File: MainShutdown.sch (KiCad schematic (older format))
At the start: 21 parts, among them J10 CONN_2X2, J6 CONN_2X2, K1 KT12-1A, K2 G6DN 12V, Q1 SSM3K361TU,LF, Q2 TSM2312, U13 TS3704IPT, U14 CD4044, U15 CD4082, U4 EL5421T

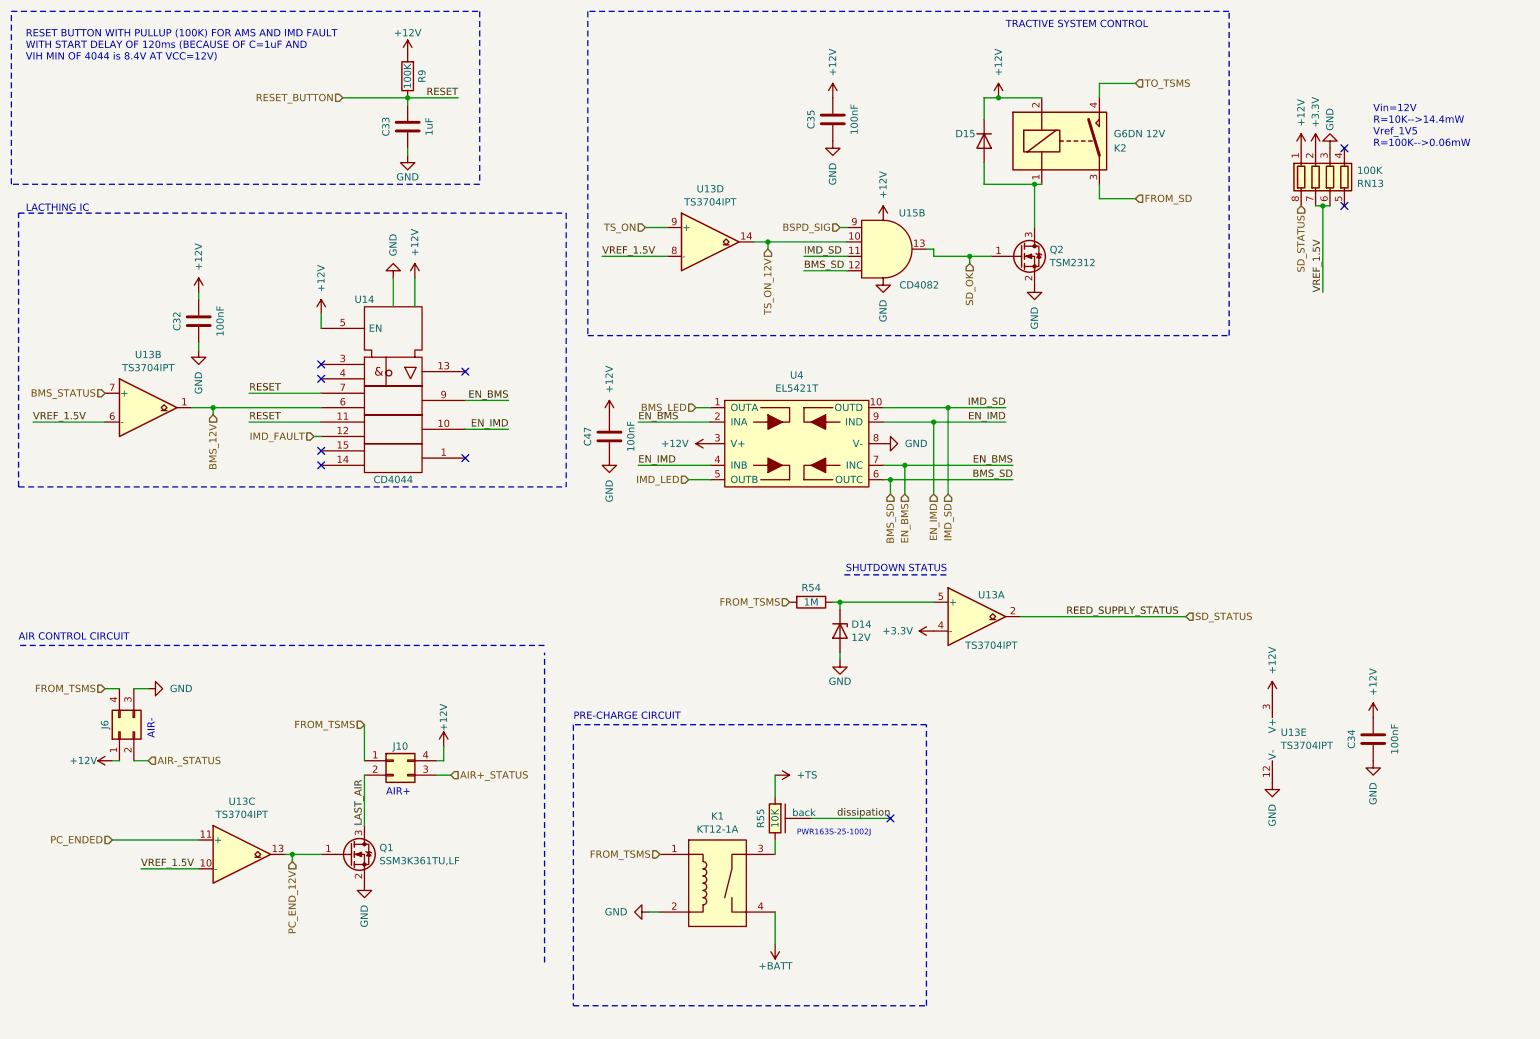
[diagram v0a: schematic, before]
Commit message: added a lot of annotations and readability in the schematic, not complete
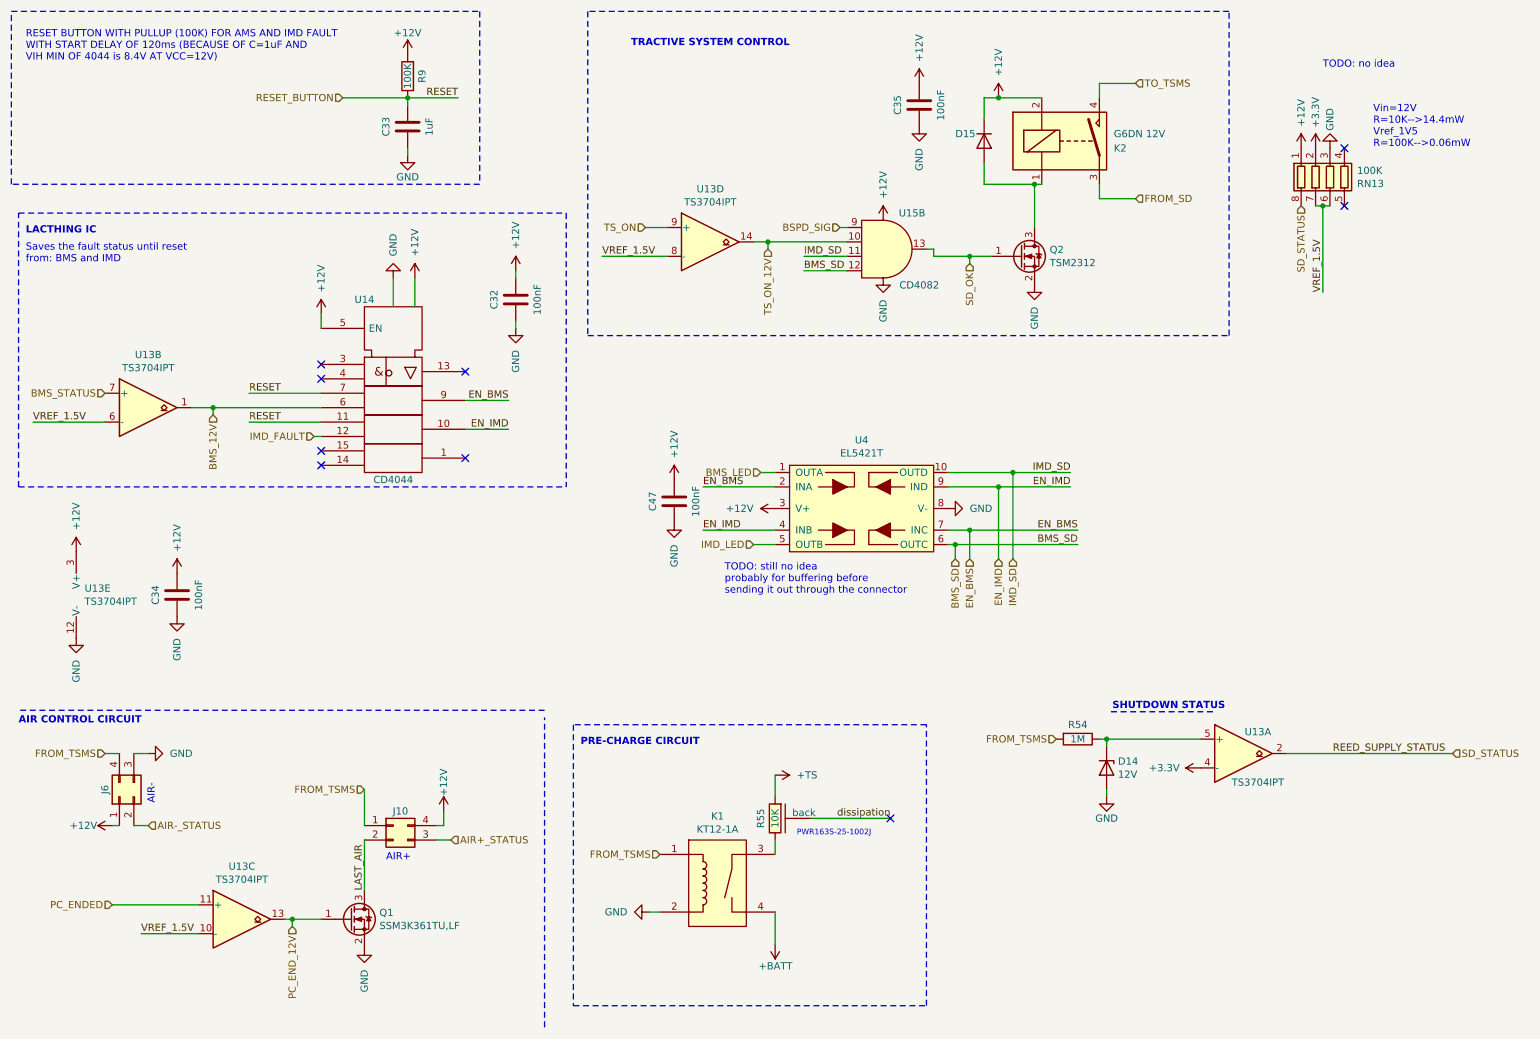
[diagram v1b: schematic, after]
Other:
- note added: "Saves the fault status until reset\nfrom: BMS and IMD"
- note added: "TODO: no idea"
- note added: "TODO: still no idea\nprobably for buffering before \nsending it out through the connector\n"
- moved on the sheet: C32, C34, C35, C47, D14, J10, J6, Q1, R54, U13A, U13C, U13E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

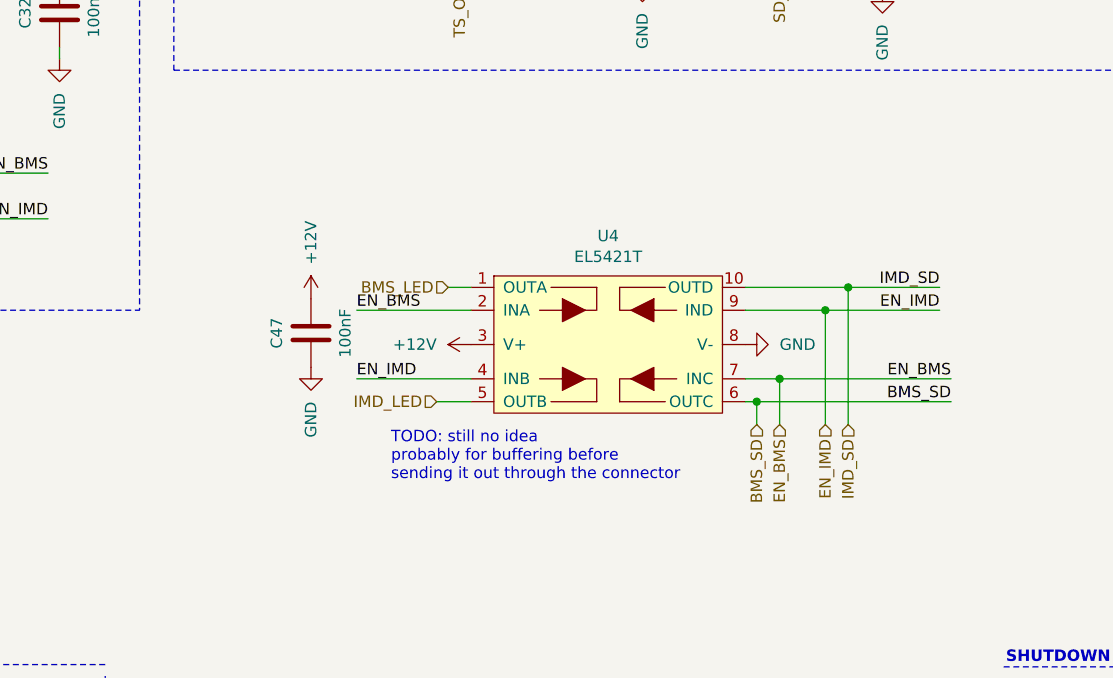
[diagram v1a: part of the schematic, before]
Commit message: Updated all to the last new v1.0.5 as printed by taba
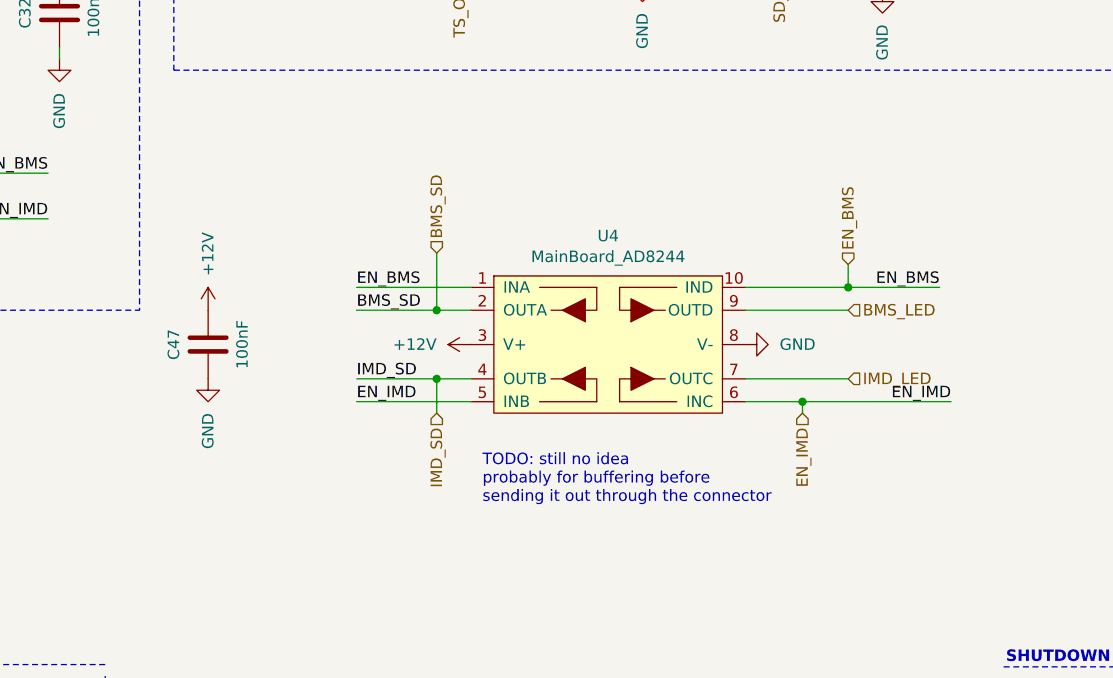
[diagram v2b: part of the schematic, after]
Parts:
- removed U4: EL5421T, Package_SO:MSOP-10_3x3mm_P0.5mm, symbol MainBoard:EL5421T
- added U4: MainBoard_AD8244, Package_SO:MSOP-10_3x3mm_P0.5mm, symbol MainBoard:MainBoard_AD8244
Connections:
- net +12V: now also U4.3 (V+)
- net BMS_LED: now also U4.9 (OUTD)
- net BMS_SD: now also U4.2 (OUTA)
- net EN_BMS: now also U4.1 (INA), U4.10 (IND)
- net EN_IMD: now also U4.5 (INB), U4.6 (INC)
- net GND: now also U4.8 (V-)
- net IMD_LED: now also U4.7 (OUTC)
- net IMD_SD: now also U4.4 (OUTB)
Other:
- moved on the sheet: C47
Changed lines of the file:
@@
 	1    0    0    -1
 $EndComp
-Text Label 5350 3950 0    50   ~ 0
+Text Label 5350 3850 0    50   ~ 0
 EN_BMS
 Wire Wire Line
-	5850 3950 5350 3950
+	5850 3950 5700 3950
 $Comp
 L power:+12V #PWR?
@@
 	0    -1   -1   0
 $EndComp
-Text Label 7900 3950 2    50   ~ 0
+Text Label 7950 4350 2    50   ~ 0
 EN_IMD
-Wire Wire Line
-	7050 3950 7400 3950
+Text Label 5350 4350 0    50   ~ 0
+EN_IMD
+Wire Wire Line
+	5850 4250 5700 4250
+Text Label 7900 3850 2    50   ~ 0
+EN_BMS
+Text Label 5350 3950 0    50   ~ 0
+BMS_SD
+Wire Wire Line
+	7050 3850 7500 3850
 Text Label 5350 4250 0    50   ~ 0
-EN_IMD
-Wire Wire Line
-	5850 4250 5350 4250
-Text Label 7950 4250 2    50   ~ 0
-EN_BMS
-Wire Wire Line
-	7050 4250 7200 4250
-Text Label 7950 4350 2    50   ~ 0
-BMS_SD
-Wire Wire Line
-	7950 4350 7100 4350
-Wire Wire Line
-	7050 3850 7500 3850
-Text Label 7900 3850 2    50   ~ 0
 IMD_SD
-Text HLabel 5750 3850 0    50   Input ~ 0
+Text HLabel 7500 3950 2    50   Input ~ 0
 BMS_LED
-Text HLabel 5700 4350 0    50   Input ~ 0
+Text HLabel 7500 4250 2    50   Input ~ 0
 IMD_LED
 Text HLabel 5050 6500 0    50   Input ~ 0
@@
 L Device:C C47
 U 1 1 5E9C316C
-P 5150 4050
-F 0 "C47" V 5000 4050 50  0000 C CNN
-F 1 "100nF" V 5300 4050 50  0000 C CNN
-F 2 "Capacitor_SMD:C_0603_1608Metric" H 5188 3900 50  0001 C CNN
-F 3 "~" H 5150 4050 50  0001 C CNN
-	1    5150 4050
+P 4700 4100
+F 0 "C47" V 4550 4100 50  0000 C CNN
+F 1 "100nF" V 4850 4100 50  0000 C CNN
+F 2 "Capacitor_SMD:C_0603_1608Metric" H 4738 3950 50  0001 C CNN
+F 3 "~" H 4700 4100 50  0001 C CNN
+	1    4700 4100
 	1    0    0    -1
 $EndComp
@@
 L power:GND #PWR0194
 U 1 1 5E9C3172
-P 5150 4200
-F 0 "#PWR0194" H 5150 3950 50  0001 C CNN
-F 1 "GND" V 5150 4050 50  0000 R CNN
-F 2 "" H 5150 4200 50  0001 C CNN
-F 3 "" H 5150 4200 50  0001 C CNN
-	1    5150 4200
+P 4700 4250
+F 0 "#PWR0194" H 4700 4000 50  0001 C CNN
+F 1 "GND" V 4700 4100 50  0000 R CNN
+F 2 "" H 4700 4250 50  0001 C CNN
+F 3 "" H 4700 4250 50  0001 C CNN
+	1    4700 4250
 	1    0    0    -1
 $EndComp
@@
 L power:+12V #PWR?
 U 1 1 5E9C3178
-P 5150 3900
+P 4700 3950
 AR Path="/5E9C3178" Ref="#PWR?"  Part="1"
 AR Path="/5B045B0D/5E9C3178" Ref="#PWR0195"  Part="1"
-F 0 "#PWR0195" H 5150 3750 50  0001 C CNN
-F 1 "+12V" V 5150 4050 50  0000 L CNN
-F 2 "" H 5150 3900 50  0001 C CNN
-F 3 "" H 5150 3900 50  0001 C CNN
-	1    5150 3900
+F 0 "#PWR0195" H 4700 3800 50  0001 C CNN
+F 1 "+12V" V 4700 4100 50  0000 L CNN
+F 2 "" H 4700 3950 50  0001 C CNN
+F 3 "" H 4700 3950 50  0001 C CNN
+	1    4700 3950
 	1    0    0    -1
 $EndComp
@@
 $EndComp
 Wire Wire Line
-	5700 4350 5850 4350
-Wire Wire Line
-	5750 3850 5850 3850
-Wire Wire Line
 	1250 6850 1850 6850
 Text HLabel 7200 2400 3    50   Input ~ 0
@@
 Wire Wire Line
 	7200 2400 7200 2350
-Text HLabel 7200 4450 3    50   Input ~ 0
+Text HLabel 7500 3750 1    50   Input ~ 0
 EN_BMS
-Text HLabel 7400 4450 3    50   Input ~ 0
+Text HLabel 7300 4400 3    50   Input ~ 0
 EN_IMD
-Text HLabel 7500 4450 3    50   Input ~ 0
+Text HLabel 5700 4400 3    50   Input ~ 0
 IMD_SD
-Text HLabel 7100 4450 3    50   Input ~ 0
+Text HLabel 5700 3700 1    50   Input ~ 0
 BMS_SD
 Text HLabel 2500 7000 3    50   Input ~ 0
@@
 Wire Wire Line
 	6950 2350 7200 2350
-Wire Wire Line
-	7500 4450 7500 3850
 Connection ~ 7500 3850
 Wire Wire Line
 	7500 3850 7900 3850
-Wire Wire Line
-	7400 4450 7400 3950
-Connection ~ 7400 3950
-Wire Wire Line
-	7400 3950 7900 3950
-Wire Wire Line
-	7200 4450 7200 4250
-Connection ~ 7200 4250
-Wire Wire Line
-	7200 4250 7950 4250
-Wire Wire Line
-	7100 4450 7100 4350
-Connection ~ 7100 4350
-Wire Wire Line
-	7100 4350 7050 4350
 Connection ~ 2500 6950
-$Comp
-L MainBoard:EL5421T U4
-U 1 1 5EDC344C
-P 6450 4100
-AR Path="/5EDC344C" Ref="U4"  Part="1"
-AR Path="/5B045B0D/5EDC344C" Ref="U4"  Part="1"
-F 0 "U4" H 6450 4575 50  0000 C CNN
-F 1 "EL5421T" H 6450 4484 50  0000 C CNN
-F 2 "Package_SO:MSOP-10_3x3mm_P0.5mm" H 5500 4650 50  0001 C CNN
-F 3 "https://www.renesas.com/us/en/www/doc/datasheet/el5421t.pdf" H 5500 4650 50  0001 C CNN
-F 4 "https://www.mouser.it/ProductDetail/Renesas-Intersil/EL5421TIYZ?qs=cbl4%252BYHJGOHzIQZSa4r%2FVQ%3D%3D" H 6450 4100 50  0001 C CNN "Mouser"
-	1    6450 4100
-	1    0    0    -1
-$EndComp
 Text Notes 10000 1600 0    50   ~ 0
 Vin=12V\nR=10K-->14.4mW\nVref_1V5\nR=100K-->0.06mW
@@
 Text Notes 9650 1050 0    50   ~ 0
 TODO: no idea
-Text Notes 5500 4700 0    50   ~ 0
+Text Notes 5900 4800 0    50   ~ 0
 TODO: still no idea\nprobably for buffering before \nsending it out through the connector\n
+$Comp
+L MainBoard:MainBoard_AD8244 U4
+U 1 1 5FDD50DE
+P 6450 4100
+F 0 "U4" H 6450 4575 50  0000 C CNN
+F 1 "MainBoard_AD8244" H 6450 4484 50  0000 C CNN
+F 2 "Package_SO:MSOP-10_3x3mm_P0.5mm" H 5500 4650 50  0001 C CNN
+F 3 "" H 5500 4650 50  0001 C CNN
+	1    6450 4100
+	1    0    0    -1
+$EndComp
+Wire Wire Line
+	7500 3850 7500 3750
+Wire Wire Line
+	7050 3950 7500 3950
+Wire Wire Line
+	7050 4250 7500 4250
+Wire Wire Line
+	7050 4350 7300 4350
+Wire Wire Line
+	5350 3850 5850 3850
+Wire Wire Line
+	5700 3700 5700 3950
+Connection ~ 5700 3950
+Wire Wire Line
+	5700 3950 5350 3950
+Wire Wire Line
+	5350 4350 5850 4350
+Wire Wire Line
+	5700 4400 5700 4250
+Connection ~ 5700 4250
+Wire Wire Line
+	5700 4250 5350 4250
+Wire Wire Line
+	7300 4400 7300 4350
+Connection ~ 7300 4350
+Wire Wire Line
+	7300 4350 7950 4350
 $EndSCHEMATC
